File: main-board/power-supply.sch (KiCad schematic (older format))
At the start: 22 parts, among them P3 IEC60320 C7, Q1 Q_NMOS_DGS, U2 AME40-12SMAZ, U3 ROM1205S, U4 AMS1117

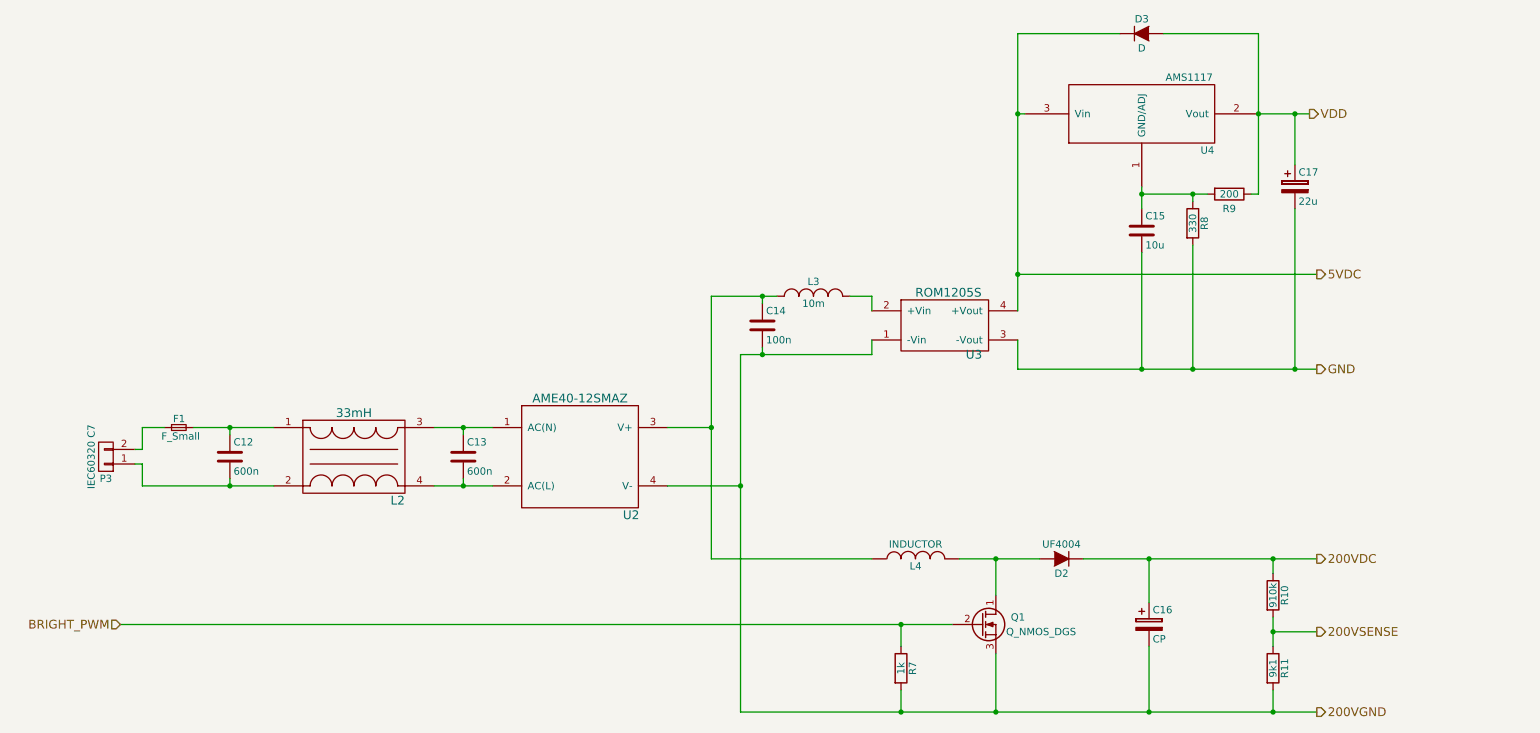
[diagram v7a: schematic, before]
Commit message: #1 - Poprawienie otoczenia ukladow od zasilania; tolerancja 1% rezystorow dzielnika pomiarowego; usuniecie kondensatora filtrujacego wyjscie z enkodera; oddalenie od siebie linii (przeniesienie 200VSENSE i BRIGHTPWM); odseparowanie I2C podciagnietej do 3,3V i 5V (po stronie GPIO Expandera) MOSFETami
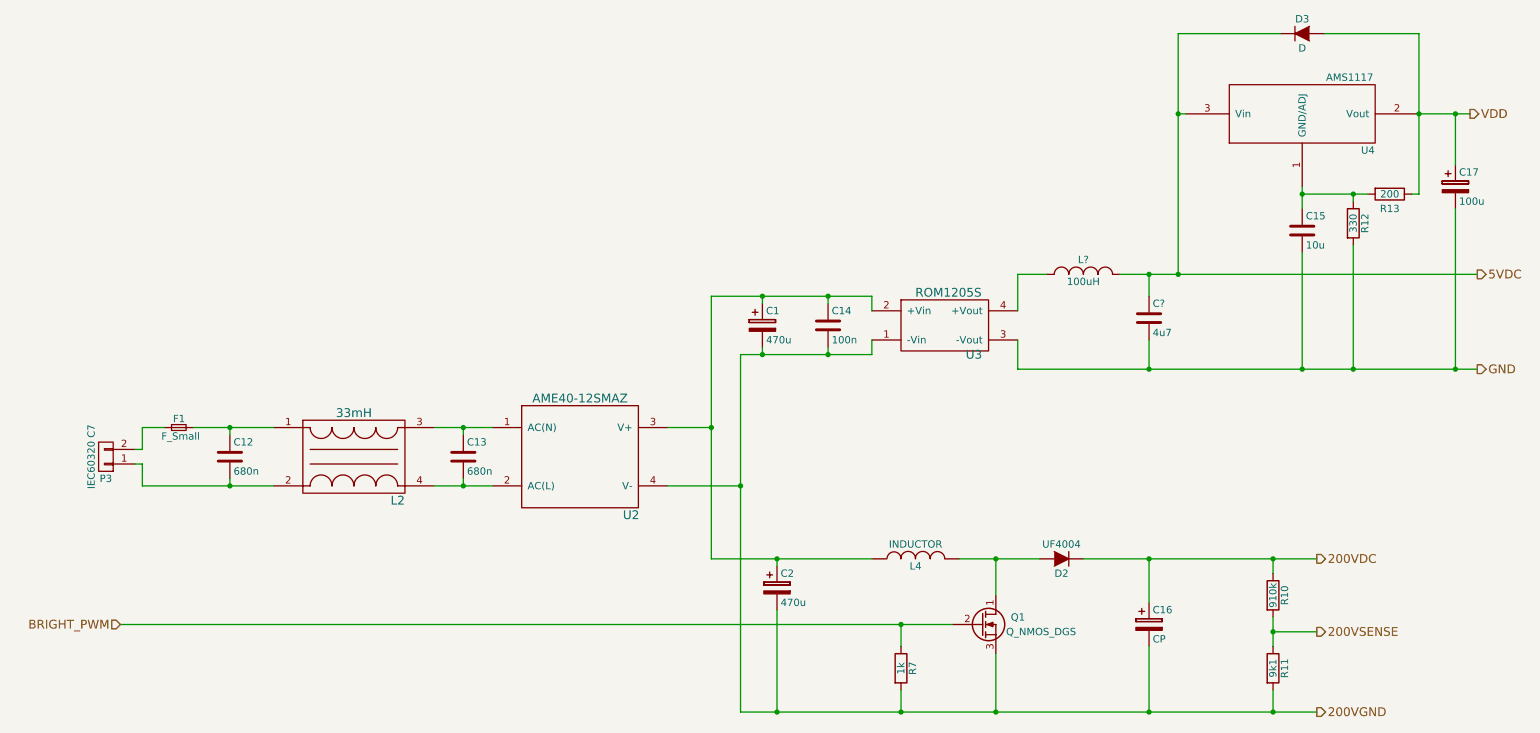
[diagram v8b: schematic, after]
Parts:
- removed L3: 10m, symbol INDUCTOR_SMALL
- added C1, C2: 470u, symbol CP
- added C?: 4u7, symbol C
- added L?: 100uH, symbol INDUCTOR_SMALL
- C12, C13: value 600n -> 680n
- C17: value 22u -> 100u
- R10, R11: Dokładność (none) -> 1%
- renumbered R8 to R12, R9 to R13
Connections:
- net 200VGND: now also C1.2, C2.2
- net 5VDC: now also C?.1, L?.2; no longer U3.4 (+Vout)
- net GND: now also C?.2
- net at C14.1, L4.1, U2.3 (V+): now also U3.2 (+Vin), C1.1, C2.1
- new net: L?.1, U3.4 (+Vout)
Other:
- moved on the sheet: C14, C15, C17, D3, R12, R13, U4
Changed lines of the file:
@@
 P 3600 3700
 F 0 "C13" H 3625 3800 50  0000 L CNN
-F 1 "600n" H 3625 3600 50  0000 L CNN
+F 1 "680n" H 3625 3600 50  0000 L CNN
 F 2 "" H 3638 3550 50  0000 C CNN
 F 3 "" H 3600 3700 50  0000 C CNN
@@
 P 2000 3700
 F 0 "C12" H 2025 3800 50  0000 L CNN
-F 1 "600n" H 2025 3600 50  0000 L CNN
+F 1 "680n" H 2025 3600 50  0000 L CNN
 F 2 "" H 2038 3550 50  0000 C CNN
 F 3 "" H 2000 3700 50  0000 C CNN
@@
 Wire Wire Line
 	5300 4400 6400 4400
-Text HLabel 9400 1350 2    60   Output ~ 0
+Text HLabel 10500 1350 2    60   Output ~ 0
 VDD
-Text HLabel 9450 3100 2    60   Output ~ 0
+Text HLabel 10550 3100 2    60   Output ~ 0
 GND
 Text HLabel 9450 4400 2    60   Output ~ 0
@@
 Text HLabel 9450 5450 2    60   Output ~ 0
 200VGND
-Text HLabel 9450 2450 2    60   Output ~ 0
+Text HLabel 10550 2450 2    60   Output ~ 0
 5VDC
 Text HLabel 1250 4850 0    60   Input ~ 0
@@
 F 2 "" V 9080 4650 50  0000 C CNN
 F 3 "" H 9150 4650 50  0000 C CNN
+F 4 "1%" V 9150 4650 60  0001 C CNN "Dokładność"
 	1    9150 4650
 	1    0    0    -1
@@
 F 2 "" V 9080 5150 50  0000 C CNN
 F 3 "" H 9150 5150 50  0000 C CNN
+F 4 "1%" V 9150 5150 60  0001 C CNN "Dokładność"
 	1    9150 5150
 	1    0    0    -1
@@
 	1    0    0    -1
 $EndComp
-$Comp
-L INDUCTOR_SMALL L3
-U 1 1 5826597D
-P 6000 2600
-F 0 "L3" H 6000 2700 50  0000 C CNN
-F 1 "10m" H 6000 2550 50  0000 C CNN
-F 2 "" H 6000 2600 50  0000 C CNN
-F 3 "" H 6000 2600 50  0000 C CNN
-	1    6000 2600
-	1    0    0    -1
-$EndComp
-Wire Wire Line
-	5300 2600 5750 2600
-Wire Wire Line
-	5650 2600 5650 2650
-Connection ~ 5650 2600
-Wire Wire Line
-	6250 2600 6400 2600
+Wire Wire Line
+	5300 2600 6400 2600
+Wire Wire Line
+	6100 2600 6100 2650
+Connection ~ 6100 2600
 Wire Wire Line
 	6400 2600 6400 2700
@@
 L C C14
 U 1 1 582658FD
+P 6100 2800
+F 0 "C14" H 6125 2900 50  0000 L CNN
+F 1 "100n" H 6125 2700 50  0000 L CNN
+F 2 "" H 6138 2650 50  0000 C CNN
+F 3 "" H 6100 2800 50  0000 C CNN
+	1    6100 2800
+	1    0    0    -1
+$EndComp
+Wire Wire Line
+	5500 3000 6400 3000
+Wire Wire Line
+	6100 3000 6100 2950
+Wire Wire Line
+	6400 3000 6400 2900
+Connection ~ 6100 3000
+Wire Wire Line
+	8500 800  8500 2450
+Wire Wire Line
+	8100 2450 10550 2450
+Wire Wire Line
+	7400 2900 7400 3100
+Wire Wire Line
+	7400 3100 10550 3100
+Wire Wire Line
+	8550 1350 8500 1350
+$Comp
+L D D3
+U 1 1 58272621
+P 9350 800
+F 0 "D3" H 9350 900 50  0000 C CNN
+F 1 "D" H 9350 700 50  0000 C CNN
+F 2 "" H 9350 800 50  0000 C CNN
+F 3 "" H 9350 800 50  0000 C CNN
+	1    9350 800
+	1    0    0    -1
+$EndComp
+Wire Wire Line
+	10150 800  10150 1900
+Wire Wire Line
+	10150 800  9500 800
+Wire Wire Line
+	9200 800  8500 800
+$Comp
+L AMS1117 U4
+U 1 1 582722A0
+P 9350 1350
+F 0 "U4" H 9800 1100 50  0000 C CNN
+F 1 "AMS1117" H 9675 1600 50  0000 C CNN
+F 2 "" H 9350 1350 60  0001 C CNN
+F 3 "" H 9350 1350 60  0001 C CNN
+	1    9350 1350
+	1    0    0    -1
+$EndComp
+Connection ~ 8500 1350
+$Comp
+L CP C17
+U 1 1 582730B0
+P 10400 1850
+F 0 "C17" H 10425 1950 50  0000 L CNN
+F 1 "100u" H 10425 1750 50  0000 L CNN
+F 2 "" H 10438 1700 50  0000 C CNN
+F 3 "" H 10400 1850 50  0000 C CNN
+	1    10400 1850
+	1    0    0    -1
+$EndComp
+$Comp
+L R R13
+U 1 1 582732A5
+P 9950 1900
+F 0 "R13" V 10050 1900 50  0000 C CNN
+F 1 "200" V 9950 1900 50  0000 C CNN
+F 2 "" V 9880 1900 50  0000 C CNN
+F 3 "" H 9950 1900 50  0000 C CNN
+	1    9950 1900
+	0    1    1    0
+$EndComp
+$Comp
+L R R12
+U 1 1 58273352
+P 9700 2100
+F 0 "R12" V 9780 2100 50  0000 C CNN
+F 1 "330" V 9700 2100 50  0000 C CNN
+F 2 "" V 9630 2100 50  0000 C CNN
+F 3 "" H 9700 2100 50  0000 C CNN
+	1    9700 2100
+	1    0    0    -1
+$EndComp
+$Comp
+L C C15
+U 1 1 58273455
+P 9350 2150
+F 0 "C15" H 9375 2250 50  0000 L CNN
+F 1 "10u" H 9375 2050 50  0000 L CNN
+F 2 "" H 9388 2000 50  0000 C CNN
+F 3 "" H 9350 2150 50  0000 C CNN
+	1    9350 2150
+	1    0    0    -1
+$EndComp
+Wire Wire Line
+	9350 1850 9350 2000
+Wire Wire Line
+	9350 2300 9350 3100
+Connection ~ 9350 3100
+Wire Wire Line
+	9350 1900 9800 1900
+Connection ~ 9350 1900
+Wire Wire Line
+	9700 1900 9700 1950
+Connection ~ 9700 1900
+Wire Wire Line
+	9700 2250 9700 3100
+Connection ~ 9700 3100
+Wire Wire Line
+	10150 1900 10100 1900
+Connection ~ 10150 1350
+Wire Wire Line
+	10150 1350 10500 1350
+Wire Wire Line
+	10400 1350 10400 1700
+Connection ~ 10400 1350
+Wire Wire Line
+	10400 2000 10400 3100
+Connection ~ 10400 3100
+$Comp
+L CP C1
+U 1 1 582F7B7F
 P 5650 2800
-F 0 "C14" H 5675 2900 50  0000 L CNN
-F 1 "100n" H 5675 2700 50  0000 L CNN
+F 0 "C1" H 5675 2900 50  0000 L CNN
+F 1 "470u" H 5675 2700 50  0000 L CNN
 F 2 "" H 5688 2650 50  0000 C CNN
 F 3 "" H 5650 2800 50  0000 C CNN
+F 4 "Tantalowe" H 5650 2800 60  0001 C CNN "Rodzaj"
 	1    5650 2800
 	1    0    0    -1
 $EndComp
 Wire Wire Line
-	5500 3000 6400 3000
-Wire Wire Line
-	5650 3000 5650 2950
-Wire Wire Line
-	6400 3000 6400 2900
+	5650 2650 5650 2600
+Connection ~ 5650 2600
+Wire Wire Line
+	5650 2950 5650 3000
 Connection ~ 5650 3000
-Wire Wire Line
-	7400 800  7400 2700
-Wire Wire Line
-	7400 2450 9450 2450
-Wire Wire Line
-	7400 2900 7400 3100
-Wire Wire Line
-	7400 3100 9450 3100
-Wire Wire Line
-	7450 1350 7400 1350
-Connection ~ 7400 2450
-$Comp
-L D D3
-U 1 1 58272621
-P 8250 800
-F 0 "D3" H 8250 900 50  0000 C CNN
-F 1 "D" H 8250 700 50  0000 C CNN
-F 2 "" H 8250 800 50  0000 C CNN
-F 3 "" H 8250 800 50  0000 C CNN
-	1    8250 800
-	1    0    0    -1
-$EndComp
-Wire Wire Line
-	9050 800  9050 1900
-Wire Wire Line
-	9050 800  8400 800
-Wire Wire Line
-	8100 800  7400 800
-$Comp
-L AMS1117 U4
-U 1 1 582722A0
-P 8250 1350
-F 0 "U4" H 8700 1100 50  0000 C CNN
-F 1 "AMS1117" H 8575 1600 50  0000 C CNN
-F 2 "" H 8250 1350 60  0001 C CNN
-F 3 "" H 8250 1350 60  0001 C CNN
-	1    8250 1350
-	1    0    0    -1
-$EndComp
-Connection ~ 7400 1350
-$Comp
-L CP C17
-U 1 1 582730B0
-P 9300 1850
-F 0 "C17" H 9325 1950 50  0000 L CNN
-F 1 "22u" H 9325 1750 50  0000 L CNN
-F 2 "" H 9338 1700 50  0000 C CNN
-F 3 "" H 9300 1850 50  0000 C CNN
-	1    9300 1850
-	1    0    0    -1
-$EndComp
-$Comp
-L R R9
-U 1 1 582732A5
-P 8850 1900
-F 0 "R9" V 8950 1900 50  0000 C CNN
-F 1 "200" V 8850 1900 50  0000 C CNN
-F 2 "" V 8780 1900 50  0000 C CNN
-F 3 "" H 8850 1900 50  0000 C CNN
-	1    8850 1900
-	0    1    1    0
-$EndComp
-$Comp
-L R R8
-U 1 1 58273352
-P 8600 2100
-F 0 "R8" V 8680 2100 50  0000 C CNN
-F 1 "330" V 8600 2100 50  0000 C CNN
-F 2 "" V 8530 2100 50  0000 C CNN
-F 3 "" H 8600 2100 50  0000 C CNN
-	1    8600 2100
-	1    0    0    -1
-$EndComp
-$Comp
-L C C15
-U 1 1 58273455
-P 8250 2150
-F 0 "C15" H 8275 2250 50  0000 L CNN
-F 1 "10u" H 8275 2050 50  0000 L CNN
-F 2 "" H 8288 2000 50  0000 C CNN
-F 3 "" H 8250 2150 50  0000 C CNN
-	1    8250 2150
-	1    0    0    -1
-$EndComp
-Wire Wire Line
-	8250 1850 8250 2000
-Wire Wire Line
-	8250 2300 8250 3100
-Connection ~ 8250 3100
-Wire Wire Line
-	8250 1900 8700 1900
-Connection ~ 8250 1900
-Wire Wire Line
-	8600 1900 8600 1950
-Connection ~ 8600 1900
-Wire Wire Line
-	8600 2250 8600 3100
-Connection ~ 8600 3100
-Wire Wire Line
-	9050 1900 9000 1900
-Connection ~ 9050 1350
-Wire Wire Line
-	9050 1350 9400 1350
-Wire Wire Line
-	9300 1350 9300 1700
-Connection ~ 9300 1350
-Wire Wire Line
-	9300 2000 9300 3100
-Connection ~ 9300 3100
+$Comp
+L CP C2
+U 1 1 582F81ED
+P 5750 4600
+F 0 "C2" H 5775 4700 50  0000 L CNN
+F 1 "470u" H 5775 4500 50  0000 L CNN
+F 2 "" H 5788 4450 50  0000 C CNN
+F 3 "" H 5750 4600 50  0000 C CNN
+F 4 "Tantalowe" H 5750 4600 60  0001 C CNN "Rodzaj"
+	1    5750 4600
+	1    0    0    -1
+$EndComp
+Wire Wire Line
+	5750 4450 5750 4400
+Connection ~ 5750 4400
+Wire Wire Line
+	5750 4750 5750 5450
+Connection ~ 5750 5450
+$Comp
+L INDUCTOR_SMALL L?
+U 1 1 582FA66C
+P 7850 2450
+F 0 "L?" H 7850 2550 50  0000 C CNN
+F 1 "100uH" H 7850 2400 50  0000 C CNN
+F 2 "" H 7850 2450 50  0000 C CNN
+F 3 "" H 7850 2450 50  0000 C CNN
+	1    7850 2450
+	1    0    0    -1
+$EndComp
+$Comp
+L C C?
+U 1 1 582FAA04
+P 8300 2750
+F 0 "C?" H 8325 2850 50  0000 L CNN
+F 1 "4u7" H 8325 2650 50  0000 L CNN
+F 2 "" H 8338 2600 50  0000 C CNN
+F 3 "" H 8300 2750 50  0000 C CNN
+	1    8300 2750
+	1    0    0    -1
+$EndComp
+Wire Wire Line
+	7400 2700 7400 2450
+Wire Wire Line
+	7400 2450 7600 2450
+Wire Wire Line
+	8300 2450 8300 2600
+Connection ~ 8500 2450
+Connection ~ 8300 2450
+Wire Wire Line
+	8300 2900 8300 3100
+Connection ~ 8300 3100
 $EndSCHEMATC
